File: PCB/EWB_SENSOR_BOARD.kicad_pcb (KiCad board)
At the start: 2 copper layers, 35 parts, among them J10 CES-124-01-S-S, J3 B4B-PH-K-S, J4 Conn_01x06_Pin, J9 CES-124-01-S-S, U1 ESP32-C3-WROOM-02-N4, U2 AZ1117CD-3.3TRG1, U3 AP64500SP-13, Y1 ABS07-32.768KHZ-T

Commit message: Changed LDO to buck, found capacitors and inductors, added bulk capacitance
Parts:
- added C16: 56.0pF, Capacitor_SMD:C_0805_2012Metric, F.Cu at (100.9, 65.9)
- added C17: 2.7nF, Capacitor_SMD:C_0805_2012Metric, F.Cu at (100.9, 68.9)
- added C18: DNP, Capacitor_SMD:C_0805_2012Metric, F.Cu at (100.9, 71.9)
- added C19: 22uF, CC1210KKX7R8BB226:CAP_CC1210_YAG, F.Cu at (89.0, 61.5)
- added C2: 10.0uF, Capacitor_SMD:C_0805_2012Metric, F.Cu at (100.9, 59.9)
- added C20: 22uF, CC1210KKX7R8BB226:CAP_CC1210_YAG, F.Cu at (95.8, 64.9)
- added C21: 22uF, CC1210KKX7R8BB226:CAP_CC1210_YAG, F.Cu at (95.8, 69.2)
- added C22: 22uF, CC1210KKX7R8BB226:CAP_CC1210_YAG, F.Cu at (95.8, 73.6)
- added C23: 22uF, CC1210KKX7R8BB226:CAP_CC1210_YAG, F.Cu at (95.8, 77.9)
- added C5: 100.0nF, Capacitor_SMD:C_0805_2012Metric, F.Cu at (100.9, 62.9)
- added L2: 3.3uH, IHLP4040DZER3R3M01:IND_IHLP-4040DZ_VIS, F.Cu at (111.0, 62.5)
- added R10: 10k, Resistor_SMD:R_0805_2012Metric, F.Cu at (105.4, 71.8)
- added R11: 10.5k, Resistor_SMD:R_0805_2012Metric, F.Cu at (105.4, 74.7)
- added R12: 70k, Resistor_SMD:R_0805_2012Metric, F.Cu at (105.4, 77.7)
- added R13: 22.1K, Resistor_SMD:R_0805_2012Metric, F.Cu at (105.4, 80.6)
- added R2: 4.7k, Resistor_SMD:R_0805_2012Metric, F.Cu at (157.6, 71.5)
- added R9: 4.7k, Resistor_SMD:R_0805_2012Metric, F.Cu at (157.6, 74.5)
- added U2: AP64500SP-13, AP64500SP-13:SO-8EP_DIO, F.Cu at (111.8, 73.6)
- L1: value 3.6uH -> 3.3uH; footprint Inductor_SMD:L_0805_2012Metric -> IHLP4040DZER3R3M01:IND_IHLP-4040DZ_VIS
- moved L1 31.5 mm to (169.0, 85.0)
- moved U3 1.91 mm to (171.3, 66.0)
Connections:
- U1 pad 14: unconnected-(U1-IO19-Pad14) -> /N_ATTN
- U1 pad 15: unconnected-(U1-IO3-Pad15) -> /N_SCL
- U1 pad 16: unconnected-(U1-IO2-Pad16) -> /N_SDA
- U1 pad 7: Net-(U1-IO8) -> unconnected-(U1-IO8-Pad7)

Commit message: almost finished
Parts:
- removed C12, C18: DNP, Capacitor_SMD:C_0805_2012Metric
- removed the C2 at (149.8, 53.6)
- removed C22, C23: 22uF, CC1210KKX7R8BB226:CAP_CC1210_YAG
- removed the C5 at (149.8, 62.6)
- removed J10, J9: CES-124-01-S-S, blues-kicad-lib:CES-124-01-S-S_Fv1.2
- removed MODL1: CES-116-01-L-S, blues-kicad-lib:16PIN_254MM_Fv1.2
- removed MODR1: CES-112-01-L-S, blues-kicad-lib:12PIN_254MM_Fv1.2
- removed the R2 at (151.1, 76.0)
- removed the U2 at (131.0, 70.7)
- added C24: 100uF, EEE_FP1C101AP:CAP_EEEFP1C101AP, F.Cu at (111.0, 47.0)
- added C25: .1uF, Capacitor_SMD:C_0805_2012Metric, F.Cu at (112.5, 52.0)
- added G***: LOGO, LOGO, F.Cu at (156.8, 59.0)
- added G***: LOGO, LOGO, B.Cu at (141.5, 68.5)
- added J1: Conn_01x24_Pin, Connector_PinHeader_2.54mm:PinHeader_1x24_P2.54mm_Vertical, B.Cu at (166.0, 31.8)
- added J2: Conn_01x03_Pin, Connector_PinSocket_2.54mm:PinSocket_1x03_P2.54mm_Vertical, F.Cu at (123.0, 31.5)
- added J5: Conn_01x03_Pin, Connector_PinSocket_2.54mm:PinSocket_1x03_P2.54mm_Vertical, F.Cu at (157.5, 36.0)
- added J6: TB002-500-02BE, TB002_500_02BE:CUI_TB002-500-02BE, F.Cu at (123.0, 70.5)
- C13, C14, C15: footprint Capacitor_SMD:C_0805_2012Metric -> CC1210KKX7R8BB226:CAP_CC1210_YAG
- J4: value Conn_01x06_Pin -> Conn_01x24_Pin; footprint Connector_PinHeader_2.54mm:PinHeader_1x06_P2.54mm_Vertical -> Connector_PinHeader_2.54mm:PinHeader_1x24_P2.54mm_Vertical; moved to B.Cu
- moved C19 59.9 mm to (143.0, 87.5)
- moved C21 53.0 mm to (147.5, 81.2), turned to -90 degrees
- moved R10 51.3 mm to (155.9, 80.6)
- moved R11 51.3 mm to (155.9, 83.5)
- moved R12 51.3 mm to (155.9, 86.5)
- moved R13 51.3 mm to (155.9, 89.5)
- moved C16 51.3 mm to (151.5, 74.7)
- moved C17 51.3 mm to (151.5, 77.7)
- moved C20 50.7 mm to (143.0, 83.5)
- moved R1 45.6 mm to (126.0, 35.0), turned to 90 degrees
- moved L2 43.2 mm to (139.5, 95.0)
- moved C2 42.1 mm to (137.0, 81.5)
- moved R5 41.9 mm to (135.0, 74.5), turned to 180 degrees
- moved J4 40.6 mm to (118.0, 31.7), turned to 180 degrees
- moved C5 40.4 mm to (135.2, 84.2)
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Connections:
- C5 pad 2: /SW -> /SW_1
- J3 pad 3: /SNS_RX -> /SNS_TX
- J3 pad 4: /SNS_TX -> /SNS_RX
- J4 pad 1: RESET -> unconnected-(J4-Pin_1-Pad1)
- J4 pad 2: +3.3V -> unconnected-(J4-Pin_2-Pad2)
- J4 pad 3: /ESP_TXD -> unconnected-(J4-Pin_3-Pad3)
- J4 pad 4: GND -> unconnected-(J4-Pin_4-Pad4)
- J4 pad 5: /ESP_RXD -> unconnected-(J4-Pin_5-Pad5)
- J4 pad 6: /ESP_IO0 -> unconnected-(J4-Pin_6-Pad6)
- L2 pad 1: /SW -> /SW_1
- R12 pad 1: /FB -> /FB_1
- R13 pad 2: /FB -> /FB_1
- U1 pad 14: /N_ATTN -> unconnected-(U1-IO19-Pad14)
- U1 pad 7: unconnected-(U1-IO8-Pad7) -> /N_ATTN
- U2 pad 5: /FB -> /FB_1
- U2 pad 8: /SW -> /SW_1
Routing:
- net +3.3V: track 0.00 -> 68.7 mm, vias 0 -> 2
- net /N_SDA: track 0.00 -> 56.5 mm, vias 0 -> 4
- net /N_SCL: track 0.00 -> 51.0 mm, vias 0 -> 4
- net +5V: track 0.00 -> 42.2 mm, vias 0 -> 2
- net /N_ATTN: track 0.00 -> 35.3 mm, vias 0 -> 2
- net /ESP_IO0: track 0.00 -> 30.1 mm
- net GND: track 0.00 -> 29.2 mm, vias 0 -> 65
- net RESET: track 0.00 -> 28.7 mm, vias 0 -> 2
- net /SNS_TX: track 0.00 -> 11.1 mm
- net /XTAL_32K_P: track 0.00 -> 11.0 mm
- net /XTAL_32K_N: track 0.00 -> 10.9 mm
- net /SNS_RX: track 0.00 -> 10.5 mm
- net /SW: track 0.00 -> 8.36 mm, vias 0 -> 2
- net /ESP_TXD: track 0.00 -> 8.23 mm
- net /ESP_RXD: track 0.00 -> 7.80 mm
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- added copper zone on F.Cu, net +3.3V
- added copper zone on F.Cu, net +5V
- added copper zone on F.Cu, net /12.8V
- added copper zone on F.Cu, net /FB
- added copper zone on F.Cu, net /SW
- added copper zone on F.Cu, net /SW_1
- added copper zone on F.Cu, net GND
- added copper zone on In1.Cu, net GND
- added copper zone on In2.Cu, net GND
- added copper zone on F.Cu, net Net-(C10-Pad2)
- added copper zone on F.Cu, net Net-(U2-BST)
- added copper zone on F.Cu, net Net-(U3-BST)
- added copper zone on F.Cu, net Net-(U3-COMP)
- added copper zone on F.Cu, net Net-(U3-RT/CLK)
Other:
- board outline added: 70.4 x 74.5 mm
- copper layers 2 -> 4
- board text removed: "F_BAT"
- board text removed: "F_SCL"
- board text removed: "F_SDA"
- board text removed: "N_EN"
- board text removed: "V+"
- board text removed: "VSOLAR"

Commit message: Finished PCB?
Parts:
- moved C16 32.0 mm to (126.8, 95.0), turned to 90 degrees
- moved R12 30.4 mm to (126.0, 92.0), turned to 180 degrees
- moved R13 29.9 mm to (126.0, 89.8)
- moved R10 29.9 mm to (126.6, 86.4), turned to 90 degrees
- moved R11 29.1 mm to (129.2, 95.0), turned to 90 degrees
- moved C17 26.2 mm to (131.8, 95.0), turned to -90 degrees
- moved G*** 10.5 mm to (140.5, 58.0)
- moved R2 7.52 mm to (156.0, 46.5)
- moved C2 4.61 mm to (132.8, 83.4), turned to 180 degrees
- moved C21 2.59 mm to (148.0, 83.8)
- moved C5 1.98 mm to (135.6, 86.2)
- moved R9 1.55 mm to (153.0, 45.6)
- moved U2 1.46 mm to (131.0, 89.2)
- moved C19 0.54 mm to (143.4, 87.9)
- moved C20 0.54 mm to (143.4, 83.9)
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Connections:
- J1 pad 3: unconnected-(J1-Pin_3-Pad3) -> /N_SDA
- J1 pad 4: unconnected-(J1-Pin_4-Pad4) -> /N_SCL
- J4 pad 12: /N_SCL -> unconnected-(J4-Pin_12-Pad12)
- J4 pad 13: /N_SDA -> unconnected-(J4-Pin_13-Pad13)
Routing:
- net +3.3V: track 68.7 -> 189.9 mm, vias 2 -> 6
- net /N_SDA: track 56.5 -> 31.2 mm, vias 4 -> 2
- net /N_SCL: track 51.0 -> 28.1 mm, vias 4 -> 2
- net /SW_1: track 0.00 -> 11.8 mm, vias 1 -> 2
- net GND: track 29.2 -> 27.3 mm, vias 65 -> 118
- net /12.8V: vias 2 -> 9
- added copper zone on F.Cu, net /FB_1
- added copper zone on F.Cu, net Net-(C17-Pad2)
- added copper zone on F.Cu, net Net-(U2-COMP)
- added copper zone on F.Cu, net Net-(U2-RT/CLK)

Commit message: Final PCB
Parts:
- removed the G*** at (140.5, 58.0)
- moved R2 5.68 mm to (150.4, 45.5)
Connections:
- J1 pad 3: /N_SDA -> unconnected-(J1-Pin_3-Pad3)
- J1 pad 4: /N_SCL -> unconnected-(J1-Pin_4-Pad4)
- J4 pad 12: unconnected-(J4-Pin_12-Pad12) -> /N_SCL
- J4 pad 13: unconnected-(J4-Pin_13-Pad13) -> /N_SDA
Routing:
- net /N_SDA: track 31.2 -> 63.6 mm, vias 2 -> 4
- net /N_SCL: track 28.1 -> 51.7 mm, vias 2 -> 4
- net +3.3V: track 189.9 -> 186.6 mm

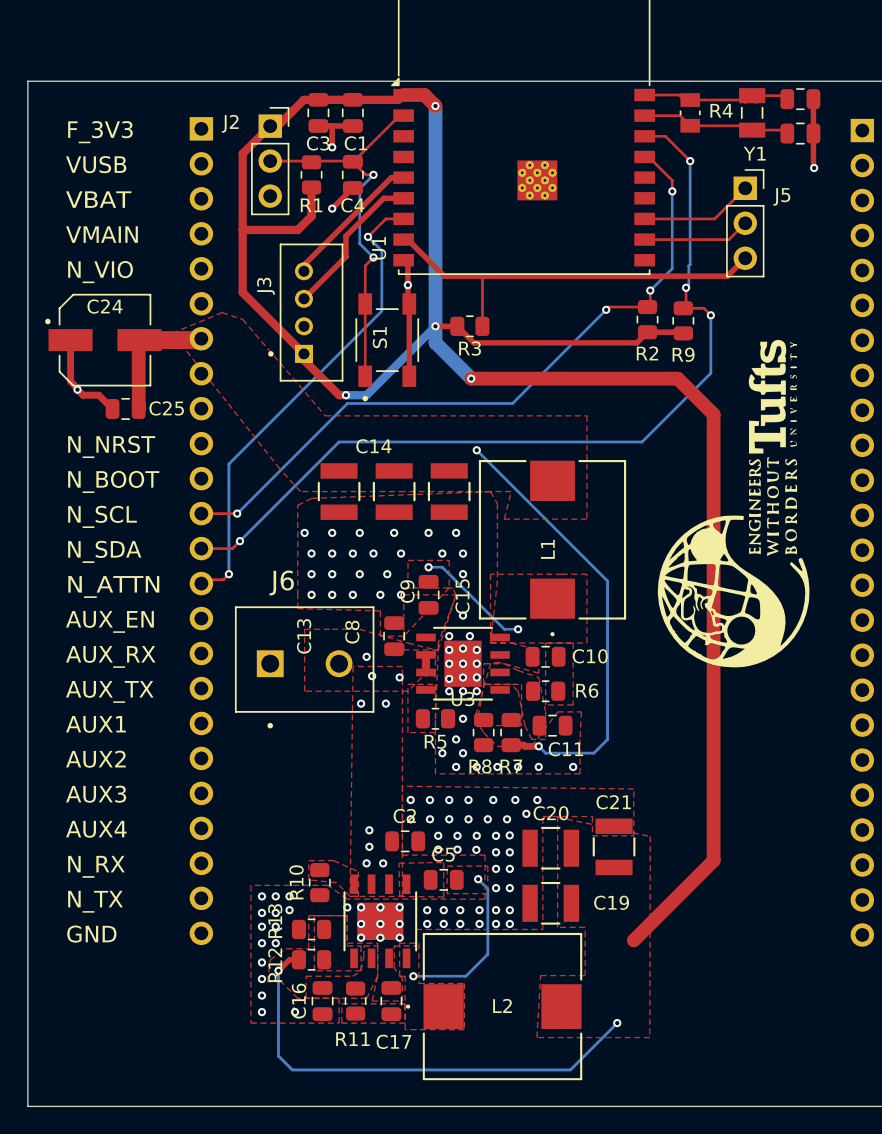
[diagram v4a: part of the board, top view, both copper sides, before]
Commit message: Changed Silk Screen to include parts values
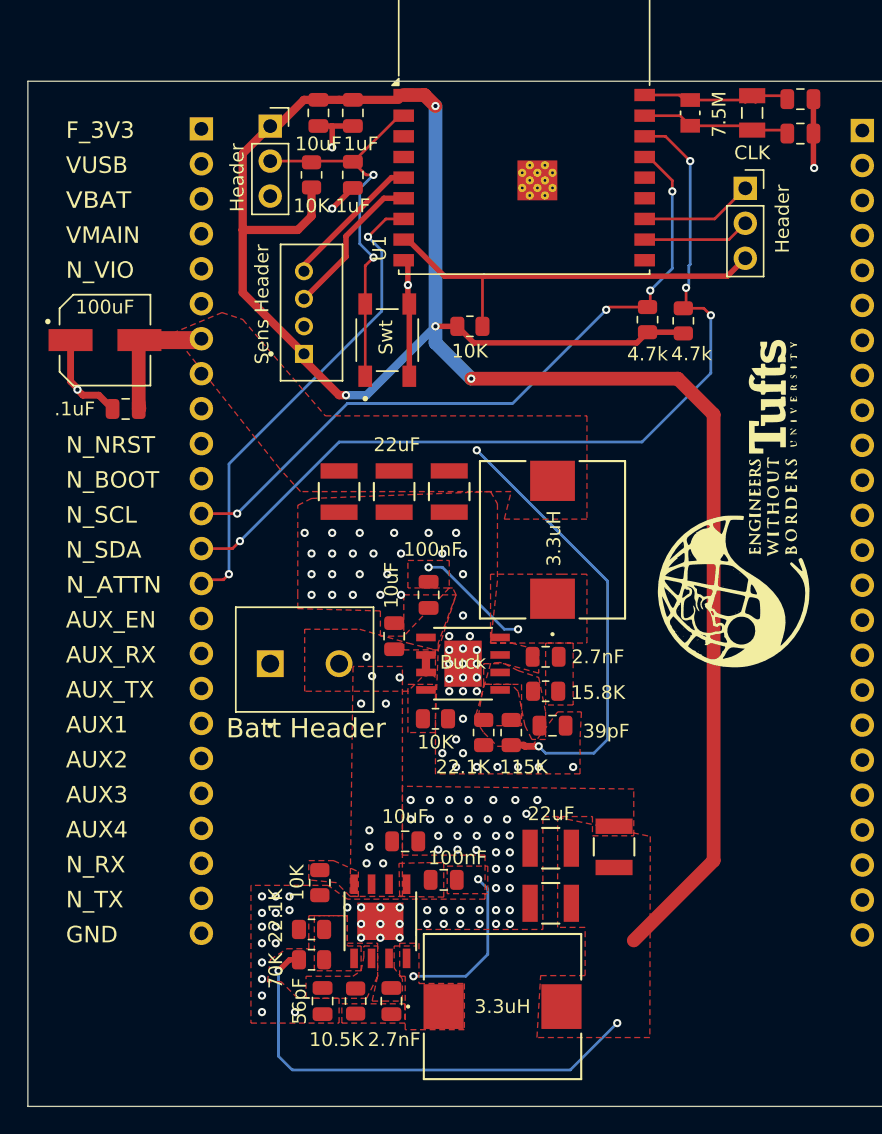
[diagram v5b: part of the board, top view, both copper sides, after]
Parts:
- Batt Header: renamed from J6
- Sens Header: renamed from J3
- renumbered C25 to .1uF, R11 to 10.5K, C5 to 100nF, C9 to 100nF, C24 to 100uF, R5 to 10K, R3 to 10K, R10 to 10K, R1 to 10K, C2 to 10uF, C3 to 10uF, C8 to 10uF, R7 to 115K, R6 to 15.8K, C1 to 1uF, C4 to 1uF, C10 to 2.7nF, C17 to 2.7nF, R8 to 22.1K, R13 to 22.1K, C20 to 22uF, C14 to 22uF, L1 to 3.3uH, L2 to 3.3uH, C11 to 39pF, R9 to 4.7k, R2 to 4.7k, C16 to 56pF, R4 to 7.5M, R12 to 70K, U3 to Buck, Y1 to CLK, J5 to Header, J2 to Header, S1 to Swt
